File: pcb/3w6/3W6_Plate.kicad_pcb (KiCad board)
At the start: 2 copper layers, 243.2 x 106 mm, 47 parts

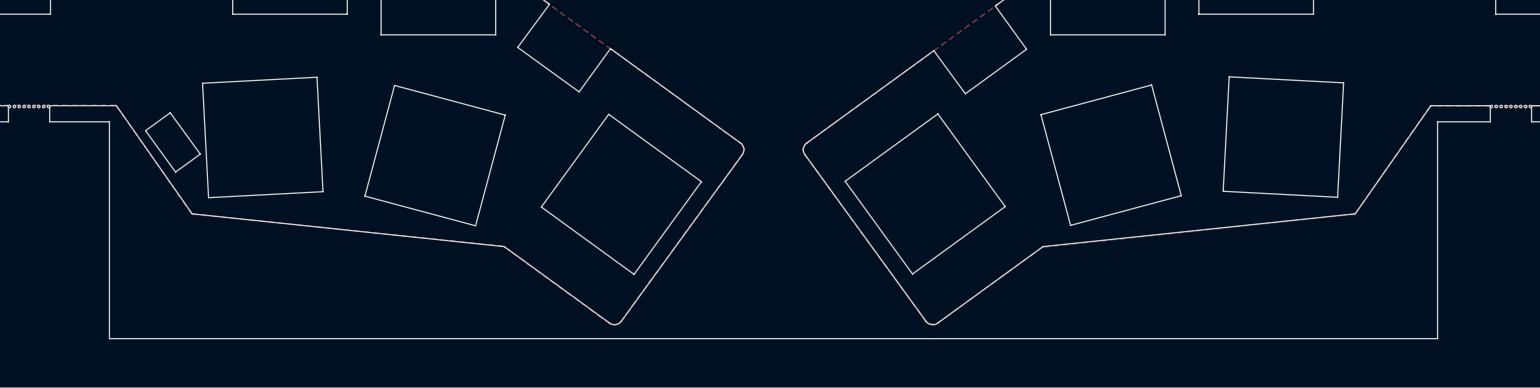
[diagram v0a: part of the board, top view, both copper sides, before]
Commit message: add: middle plate chg: rerouting whole board, to eliminate traces under middle plate chg: repositioning components to get a higher clearance in case an aluminium or steel middle plate is used.
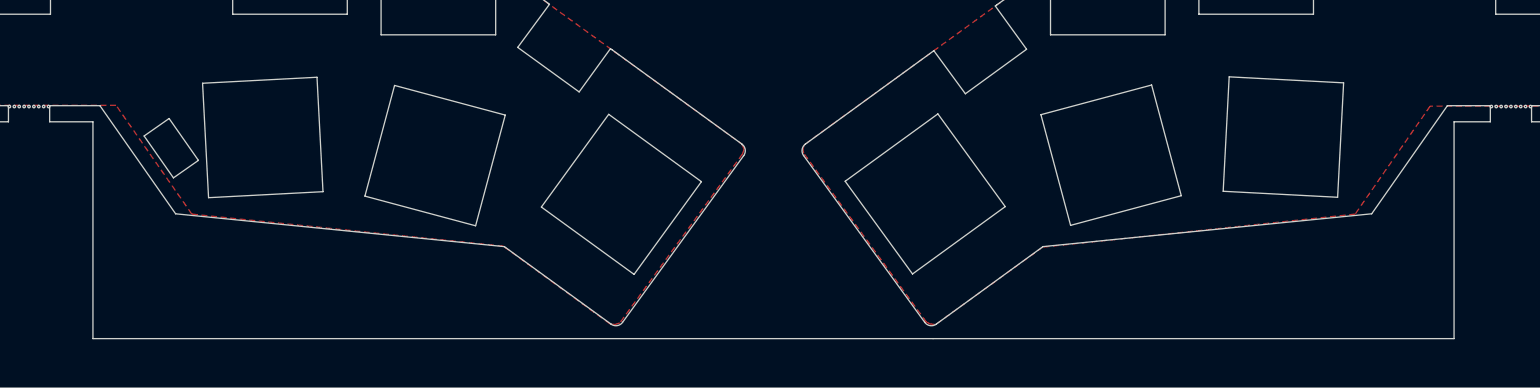
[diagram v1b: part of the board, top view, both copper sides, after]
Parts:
- removed the REF** at (276.5, 47.3)
- removed the REF** at (276.5, 64.3)
- removed the REF** at (276.5, 81.3)
- removed the REF** at (258.5, 38.3)
- removed the REF** at (240.5, 35.3)
- removed the REF** at (204.5, 40.8)
- removed the REF** at (258.5, 55.3)
- removed the REF** at (240.5, 52.3)
- removed the REF** at (222.5, 55.3)
- removed the REF** at (222.5, 72.3)
- removed the REF** at (204.5, 57.8)
- removed the REF** at (240.5, 69.3)
- removed the REF** at (123.3, 74.8)
- removed the REF** at (105.3, 55.3)
- removed the REF** at (105.3, 72.3)
- removed the REF** at (123.3, 57.8)
- removed the REF** at (87.3, 35.3)
- removed the REF** at (69.3, 55.3)
- removed the REF** at (123.3, 40.8)
- removed the REF** at (102.0, 94.2)
- removed the REF** at (122.9, 96.4)
- removed the REF** at (69.3, 38.3)
- removed the REF** at (105.3, 38.3)
- removed the REF** at (204.5, 74.8)
- removed the REF** at (145.5, 101.1)
- removed the REF** at (87.3, 69.3)
- removed the REF** at (87.3, 52.3)
- removed the REF** at (51.3, 81.3)
- removed the REF** at (69.3, 72.3)
- removed the REF** at (51.3, 64.3)
- removed the REF** at (182.3, 101.0)
- removed the REF** at (204.9, 96.3)
- removed the REF** at (225.8, 94.2)
- added REF**: Plate_Hole, Weteor:Plate_Hole, F.Cu at (276.5, 64.3)
- added REF**: Plate_Hole, Weteor:Plate_Hole, F.Cu at (276.5, 81.3)
- added REF**: Plate_Hole, Weteor:Plate_Hole, F.Cu at (258.5, 38.3)
- added REF**: Plate_Hole, Weteor:Plate_Hole, F.Cu at (240.5, 35.3)
- added REF**: Plate_Hole, Weteor:Plate_Hole, F.Cu at (204.5, 40.8)
- added REF**: Plate_Hole, Weteor:Plate_Hole, F.Cu at (258.5, 55.3)
- added REF**: Plate_Hole, Weteor:Plate_Hole, F.Cu at (240.5, 52.3)
- added REF**: Plate_Hole, Weteor:Plate_Hole, F.Cu at (222.5, 55.3)
- added REF**: Plate_Hole, Weteor:Plate_Hole, F.Cu at (222.5, 72.3)
- added REF**: Plate_Hole, Weteor:Plate_Hole, F.Cu at (204.5, 57.8)
- added REF**: Plate_Hole, Weteor:Plate_Hole, F.Cu at (240.5, 69.3)
- added REF**: Plate_Hole, Weteor:Plate_Hole, F.Cu at (123.3, 74.8)
- added REF**: Plate_Hole, Weteor:Plate_Hole, F.Cu at (105.3, 55.3)
- added REF**: Plate_Hole, Weteor:Plate_Hole, F.Cu at (105.3, 72.3)
- added REF**: Plate_Hole, Weteor:Plate_Hole, F.Cu at (123.3, 57.8)
- added REF**: Plate_Hole, Weteor:Plate_Hole, F.Cu at (87.3, 35.3)
- added REF**: Plate_Hole, Weteor:Plate_Hole, F.Cu at (69.3, 55.3)
- added REF**: Plate_Hole, Weteor:Plate_Hole, F.Cu at (123.3, 40.8)
- added REF**: Plate_Hole, Weteor:Plate_Hole, F.Cu at (122.9, 96.4)
- added REF**: Plate_Hole, Weteor:Plate_Hole, F.Cu at (102.0, 94.2)
- added REF**: Plate_Hole, Weteor:Plate_Hole, F.Cu at (69.3, 38.3)
- added REF**: Plate_Hole, Weteor:Plate_Hole, F.Cu at (105.3, 38.3)
- added REF**: Plate_Hole, Weteor:Plate_Hole, F.Cu at (204.5, 74.8)
- added REF**: Plate_Hole, Weteor:Plate_Hole, F.Cu at (145.5, 101.1)
- added REF**: Plate_Hole, Weteor:Plate_Hole, F.Cu at (87.3, 69.3)
- added REF**: Plate_Hole, Weteor:Plate_Hole, F.Cu at (87.3, 52.3)
- added REF**: Plate_Hole, Weteor:Plate_Hole, F.Cu at (51.3, 81.3)
- added REF**: Plate_Hole, Weteor:Plate_Hole, F.Cu at (69.3, 72.3)
- added REF**: Plate_Hole, Weteor:Plate_Hole, F.Cu at (51.3, 64.3)
- added REF**: Plate_Hole, Weteor:Plate_Hole, F.Cu at (182.3, 101.0)
- added REF**: Plate_Hole, Weteor:Plate_Hole, F.Cu at (204.9, 96.3)
- added REF**: Plate_Hole, Weteor:Plate_Hole, F.Cu at (225.8, 94.2)
- added REF**: Plate_Hole, Weteor:Plate_Hole, F.Cu at (276.5, 47.3)
- G***: footprint WetCorn:Logo -> Weteor:Logo
- REF**: footprint WetCorn:Logo_L -> Weteor:Logo_L
- REF** (x3): footprint WetCorn:Plate_Hole -> Weteor:Plate_Hole
- moved G*** 2.70 mm to (261.9, 85.9)
- moved REF** 2.50 mm to (70.8, 85.9)
- moved REF** 0.73 mm to (90.9, 95.5), turned to 125 degrees
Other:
- outline, holes or cut-outs redrawn

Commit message: changes for production
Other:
- outline, holes or cut-outs redrawn
